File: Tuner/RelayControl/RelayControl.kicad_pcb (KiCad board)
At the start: 2 copper layers, 99.1 x 99.6 mm, 180 parts, among them J1 Conn_01x06, J12 Conn_01x01, J13 Conn_01x01, J14 Conn_01x01, J2 Conn_02x16_Odd_Even, J3 Conn_01x06, J4 Conn_01x01, J5 Conn_01x01, J6 Conn_01x01, J7 Conn_01x01, J8 Conn_02x16_Odd_Even, J9 Conn_01x01, U1 MCP23017, U2 ULN2803A, U3 ULN2803A, U4 MCP23017, U5 ULN2803A, U6 ULN2803A

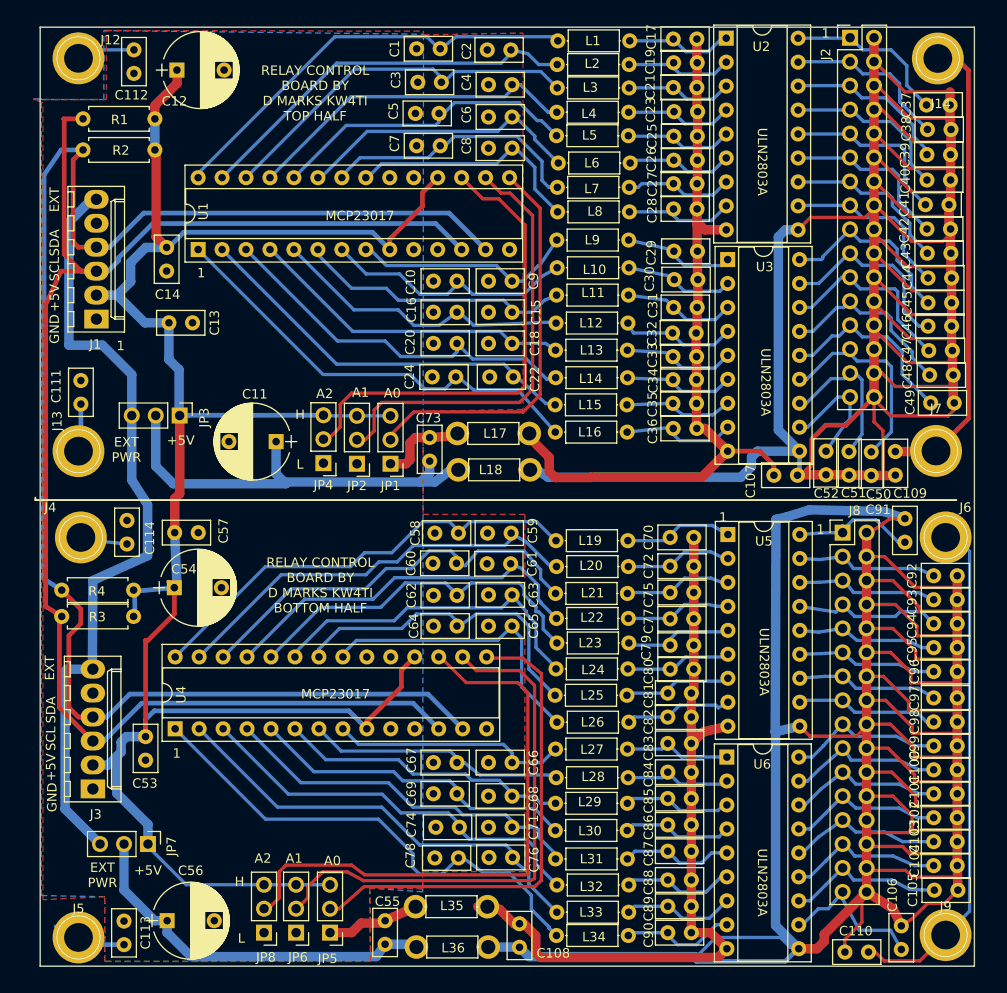
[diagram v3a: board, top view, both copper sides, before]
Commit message: JLCPCB order 09232018 - improved grounding - improved I2C cabling - NEO7M port - support for common mode chokes - relay board now has capacitors on all coils
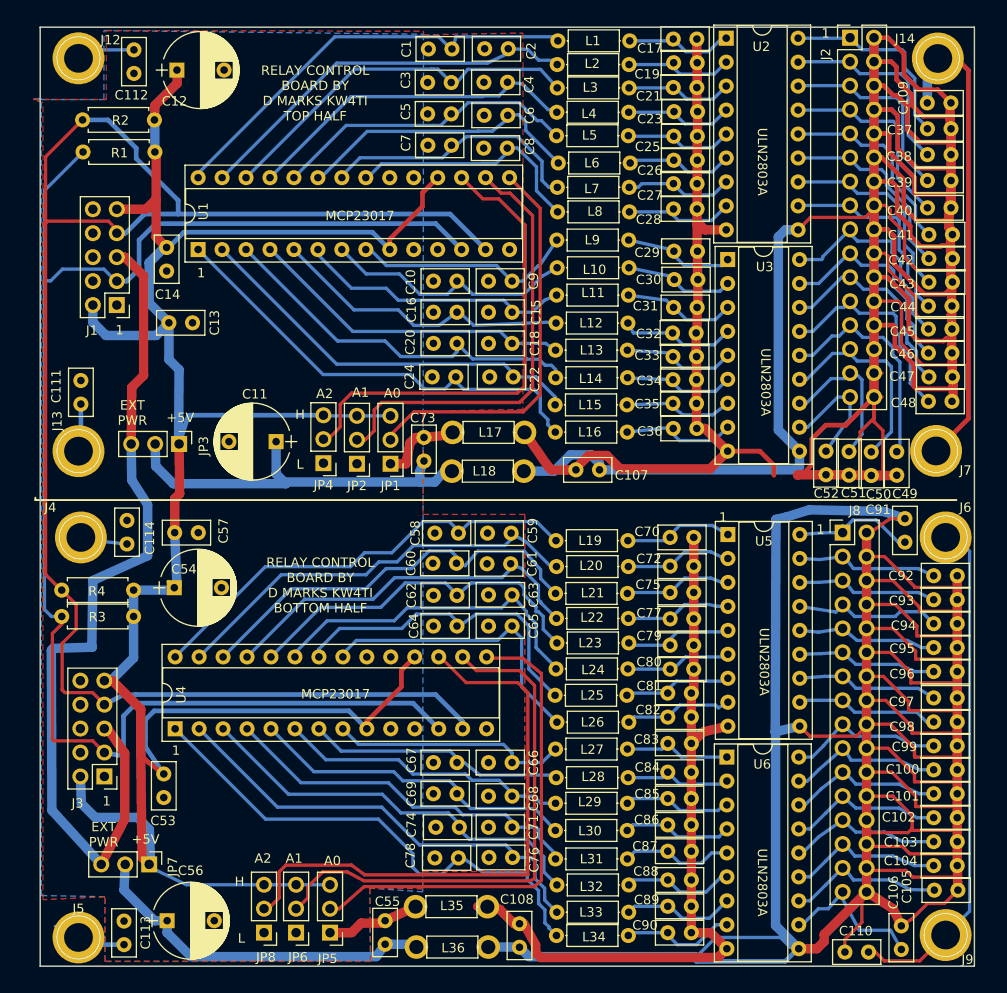
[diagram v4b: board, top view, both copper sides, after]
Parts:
- J1, J3: value Conn_01x06 -> Conn_02x05_Odd_Even; footprint Connectors_Molex:Molex_KK-6410-06_06x2.54mm_Straight -> Pin_Headers:Pin_Header_Straight_2x05_Pitch2.54mm
- moved C109 39.9 mm to (148.4, 57.7), turned to 180 degrees
- moved C107 21.0 mm to (108.6, 96.6)
- moved C49 6.30 mm to (142.6, 94.7), turned to 270 degrees
- moved C53 4.41 mm to (64.9, 131.4)
- moved R1 3.52 mm to (64.0, 62.9)
- moved C41 3.20 mm to (146.1, 71.7)
- moved R2 3.19 mm to (63.9, 59.5)
- moved C42 3.14 mm to (146.1, 74.2)
- moved C43 3.07 mm to (146.1, 76.7)
- moved JP3 3.02 mm to (66.5, 93.9)
- moved C44 2.97 mm to (146.0, 79.2)
- moved C40 2.95 mm to (145.9, 68.8)
- moved C46 2.85 mm to (146.0, 84.2)
- moved C48 2.80 mm to (146.0, 89.4)
- moved C47 2.79 mm to (146.1, 86.8)
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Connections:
- J1 pad 4: SDA -> GND
- J1 pad 5: (no net) -> EXTPWR
- J1 pad 6: EXTPWR -> GND
- J3 pad 4: SDA -> GND
- J3 pad 5: (no net) -> EXTPWR
- J3 pad 6: EXTPWR -> GND
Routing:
- net Net-(C107-Pad2): track 311.8 -> 362.5 mm
- net +5V: track 225.7 -> 252.2 mm
- net EXTPWR: track 83.3 -> 92.9 mm
- net SDA: track 166.7 -> 175.6 mm
- net SCL: track 159.1 -> 165.7 mm
- net RLYPWR: track 46.4 -> 42.5 mm
- net Net-(C49-Pad1): track 20.1 -> 23.7 mm
- net Net-(C39-Pad1): track 17.9 -> 21.5 mm
- net Net-(C38-Pad1): track 17.8 -> 21.4 mm
- net Net-(C43-Pad1): track 18.2 -> 21.6 mm
- net Net-(C48-Pad1): track 19.6 -> 23.0 mm
- net Net-(C40-Pad1): track 18.3 -> 21.6 mm
- net Net-(C37-Pad1): track 17.8 -> 21.1 mm
- net Net-(C45-Pad1): track 19.8 -> 23.1 mm
- net Net-(C44-Pad1): track 18.6 -> 21.8 mm
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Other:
- board text removed: "EXT"
- board text removed: "GND"
- board text removed: "SCL"
- board text removed: "SDA"

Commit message: Relay boards changed to have coil terminals all on same side
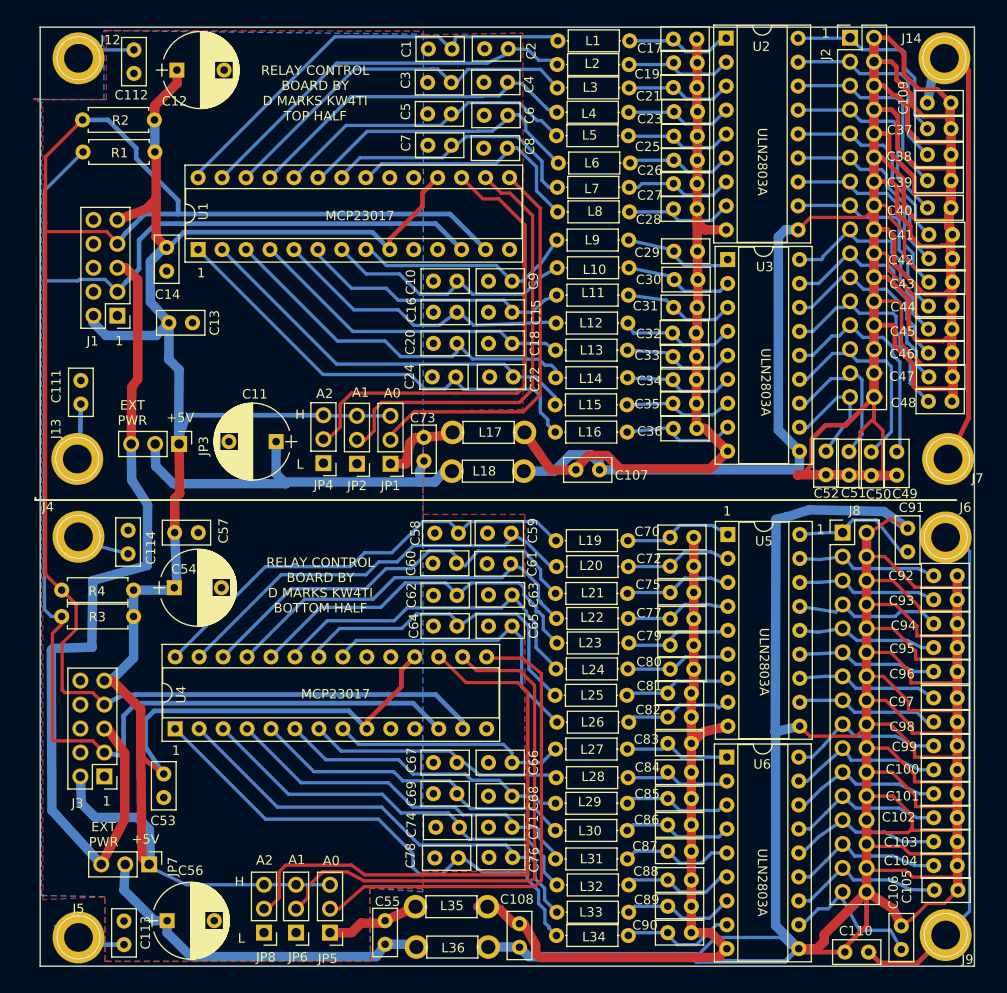
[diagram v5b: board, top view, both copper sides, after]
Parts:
- moved J7 1.53 mm to (148.1, 95.5)
- moved J1 1.13 mm to (60.0, 80.3)
- moved C91 1.06 mm to (143.8, 105.3)
- moved C114 1.05 mm to (61.1, 105.5)
- moved J13 0.84 mm to (55.8, 95.5)
- moved J14 0.70 mm to (147.7, 53.0)
- moved J4 0.26 mm to (55.9, 103.7)
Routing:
- net Net-(C100-Pad2): track 379.7 -> 386.7 mm
- net Net-(C107-Pad1): track 83.0 -> 76.4 mm
- net +5V: track 252.2 -> 251.0 mm
- net EXTPWR: track 92.9 -> 91.8 mm
- net Net-(C91-Pad1): track 13.6 -> 14.5 mm
- net Net-(C110-Pad1): track 54.6 -> 55.5 mm
- net Net-(C111-Pad2): track 5.15 -> 5.98 mm
- net Net-(C114-Pad1): track 6.46 -> 7.03 mm

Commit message: Changed over yet more to BNC
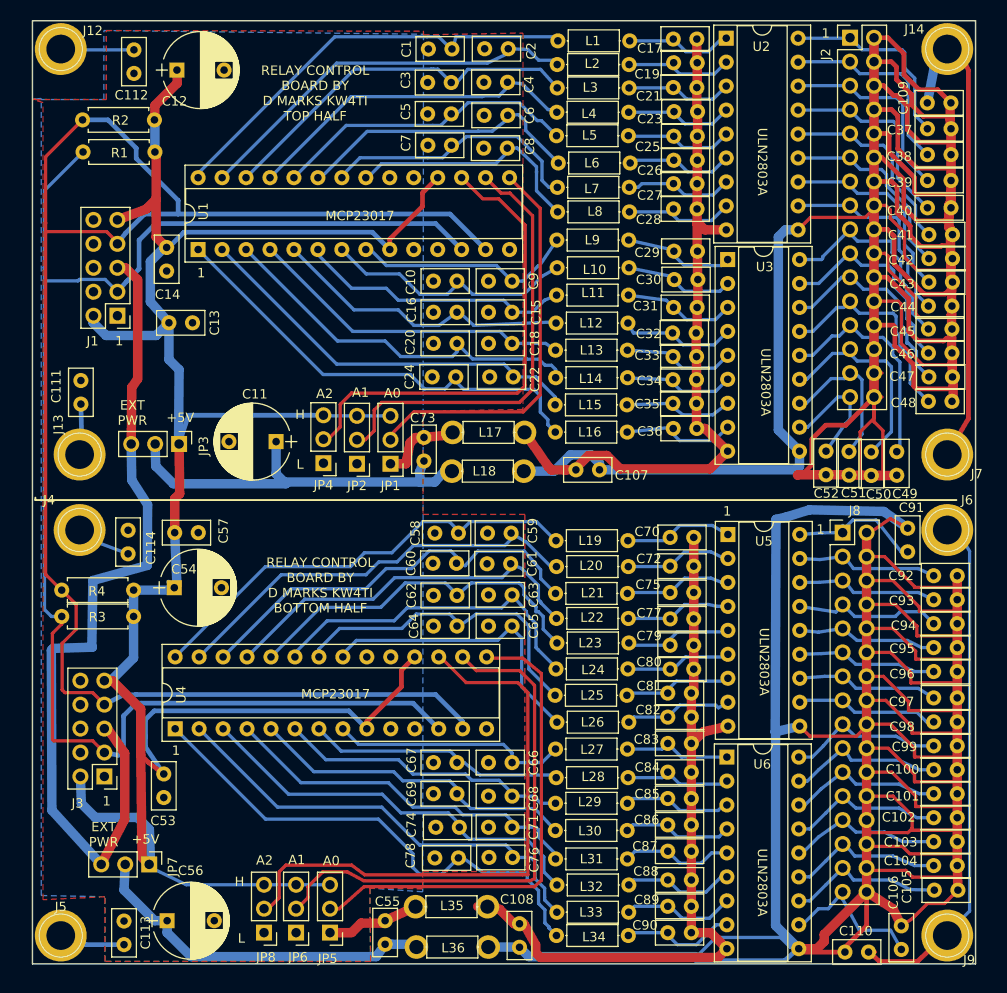
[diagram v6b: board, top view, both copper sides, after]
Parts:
- moved J12 2.12 mm to (54.0, 52.0)
- moved J5 1.89 mm to (54.0, 146.0)
- moved J14 1.03 mm to (148.0, 52.0)
- moved J6 0.80 mm to (148.0, 103.0)
- moved J4 0.73 mm to (56.0, 103.0)
- moved J13 0.53 mm to (56.0, 95.0)
- moved J7 0.47 mm to (148.0, 95.0)
- moved J9 0.18 mm to (148.0, 146.0)
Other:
- board size 99.1 x 99.6 mm -> 100 x 100 mm
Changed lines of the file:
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@@
     (links 425)
     (no_connects 0)
-    (area 48.700818 47.9952 152.57562 150.8094)
+    (area 48.700818 47.9952 152.82962 150.8094)
     (thickness 1.6)
     (drawings 37)
@@
     (pad_to_mask_clearance 0.2)
     (aux_axis_origin 0 0)
-    (grid_origin 103.632 154.0764)
     (visible_elements 7FFFFFFF)
     (pcbplotparams
@@
   )
   (module Connectors:1pin (layer F.Cu)
-    (at 55.88 52.9844)
+    (at 54 52)
     (descr "module 1 pin (ou trou mecanique de percage)")
     (tags DEV)
@@
   )
   (module Connectors:1pin (layer F.Cu)
-    (at 55.753 95.4659)
+    (at 56 95)
     (descr "module 1 pin (ou trou mecanique de percage)")
     (tags DEV)
@@
   )
   (module Connectors:1pin (layer F.Cu)
-    (at 147.701 52.9844)
+    (at 148 52)
     (descr "module 1 pin (ou trou mecanique de percage)")
     (tags DEV)
@@
   )
   (module Connectors:1pin (layer F.Cu)
-    (at 148.082 95.4659)
+    (at 148 95)
     (descr "module 1 pin (ou trou mecanique de percage)")
     (tags DEV)
@@
   )
   (module Connectors:1pin (layer F.Cu)
-    (at 55.88 103.7209)
+    (at 56 103)
     (descr "module 1 pin (ou trou mecanique de percage)")
     (tags DEV)
@@
   )
   (module Connectors:1pin (layer F.Cu)
-    (at 55.88 146.2024)
+    (at 54 146)
     (descr "module 1 pin (ou trou mecanique de percage)")
     (tags DEV)
@@
   )
   (module Connectors:1pin (layer F.Cu)
-    (at 147.828 103.7844)
+    (at 148 103)
     (descr "module 1 pin (ou trou mecanique de percage)")
     (tags DEV)
@@
   )
   (module Connectors:1pin (layer F.Cu)
-    (at 147.828 145.9484)
+    (at 148 146)
     (descr "module 1 pin (ou trou mecanique de percage)")
     (tags DEV)
@@
     )
   )
+  (gr_line (start 51 149) (end 51 49) (angle 90) (layer Edge.Cuts) (width 0.15))
+  (gr_line (start 151 149) (end 51 149) (angle 90) (layer Edge.Cuts) (width 0.15))
+  (gr_line (start 151 49) (end 151 149) (angle 90) (layer Edge.Cuts) (width 0.15))
+  (gr_line (start 51 49) (end 151 49) (angle 90) (layer Edge.Cuts) (width 0.15))
   (gr_text 1 (at 58.8645 131.7498) (layer F.SilkS)
     (effects (font (size 1 1) (thickness 0.15)))
   )
-  (gr_line (start 51.816 149.2504) (end 51.816 49.6824) (angle 90) (layer Edge.Cuts) (width 0.15))
-  (gr_line (start 150.876 149.2504) (end 51.816 149.2504) (angle 90) (layer Edge.Cuts) (width 0.15))
-  (gr_line (start 150.876 49.6824) (end 150.876 149.2504) (angle 90) (layer Edge.Cuts) (width 0.15))
-  (gr_line (start 51.816 49.6824) (end 150.876 49.6824) (angle 90) (layer Edge.Cuts) (width 0.15))
   (gr_text 1 (at 68.8848 75.7428) (layer F.SilkS)
     (effects (font (size 1 1) (thickness 0.15)))
@@
   (segment (start 120.904 148.2344) (end 121.35104 148.2344) (width 0.35) (layer B.Cu) (net 95))
   (segment (start 121.35104 148.2344) (end 121.412 148.2344) (width 0.35) (layer B.Cu) (net 95))
-  (segment (start 130.81 148.7424) (end 121.412 148.7424) (width 0.5) (layer B.Cu) (net 95))
-  (segment (start 121.412 148.7424) (end 120.904 148.2344) (width 0.5) (layer B.Cu) (net 95))
-  (segment (start 132.156 147.3964) (end 130.81 148.7424) (width 0.5) (layer B.Cu) (net 95) (status 10))
+  (segment (start 130.7592 148.6662) (end 121.3612 148.6662) (width 0.5) (layer B.Cu) (net 95))
+  (segment (start 121.3612 148.6662) (end 120.904 148.2344) (width 0.5) (layer B.Cu) (net 95))
+  (segment (start 132.156 147.3964) (end 130.7592 148.6662) (width 0.5) (layer B.Cu) (net 95) (status 10))
   (segment (start 121.412 148.2344) (end 123.444 146.2024) (width 0.35) (layer B.Cu) (net 95))
   (segment (start 131.318 147.2184) (end 132.074 147.2184) (width 0.35) (layer B.Cu) (net 95) (status 20))
@@
   (segment (start 147.701 52.9844) (end 149.6876 52.9844) (width 0.5) (layer F.Cu) (net 114) (status 30))
   (segment (start 149.6876 52.9844) (end 150.241 54.2544) (width 0.5) (layer F.Cu) (net 114) (status 10))
-  (segment (start 150.241 91.186) (end 148.082 95.4659) (width 0.5) (layer F.Cu) (net 114) (status 20))
+  (segment (start 150.241 91.186) (end 148 95) (width 0.5) (layer F.Cu) (net 114) (status 20))
   (segment (start 150.241 54.2544) (end 150.241 91.186) (width 0.5) (layer F.Cu) (net 114))
-  (segment (start 148.0166 95.5313) (end 148.082 95.4659) (width 1) (layer F.Cu) (net 114) (status 30))
+  (segment (start 147.9346 95.0654) (end 148 95) (width 1) (layer F.Cu) (net 114) (status 30))
   (segment (start 147.513 53.1724) (end 147.701 52.9844) (width 1) (layer B.Cu) (net 114) (status 30))
   (segment (start 139.6492 147.7518) (end 139.7254 147.7518) (width 0.5) (layer F.Cu) (net 115))
-  (segment (start 139.7254 147.7518) (end 140.8811 148.9075) (width 0.5) (layer F.Cu) (net 115))
-  (segment (start 144.8689 148.9075) (end 147.828 145.9484) (width 0.5) (layer F.Cu) (net 115))
-  (segment (start 140.8811 148.9075) (end 144.8689 148.9075) (width 0.5) (layer F.Cu) (net 115))
+  (segment (start 139.7254 147.7518) (end 140.8303 148.7551) (width 0.5) (layer F.Cu) (net 115))
+  (segment (start 144.8181 148.7551) (end 147.828 145.9484) (width 0.5) (layer F.Cu) (net 115))
+  (segment (start 140.8303 148.7551) (end 144.8181 148.7551) (width 0.5) (layer F.Cu) (net 115))
   (segment (start 139.6492 147.7518) (end 140.3858 147.7518) (width 0.35) (layer F.Cu) (net 115))
-  (segment (start 147.828 103.7844) (end 148.8948 103.7844) (width 0.35) (layer B.Cu) (net 115))
-  (segment (start 148.8948 103.7844) (end 150.368 105.2576) (width 0.35) (layer B.Cu) (net 115))
+  (segment (start 148 103) (end 149.0668 103) (width 0.35) (layer B.Cu) (net 115) (status 30))
+  (segment (start 149.0668 103) (end 150.368 105.2576) (width 0.35) (layer B.Cu) (net 115) (status 10))
   (segment (start 150.368 105.2576) (end 150.368 143.4084) (width 0.35) (layer B.Cu) (net 115))
   (segment (start 150.368 143.4084) (end 147.828 145.9484) (width 0.35) (layer B.Cu) (net 115))
-  (segment (start 56.134 89.6474) (end 56.007 95.2119) (width 0.5) (layer B.Cu) (net 116) (status 20))
-  (segment (start 56.007 95.2119) (end 55.753 95.4659) (width 0.5) (layer B.Cu) (net 116) (status 30))
+  (segment (start 56.134 89.6474) (end 56.254 94.746) (width 0.5) (layer B.Cu) (net 116) (status 20))
+  (segment (start 56.254 94.746) (end 56 95) (width 0.5) (layer B.Cu) (net 116) (status 30))
   (segment (start 56.134 89.6474) (end 56.134 89.7001) (width 0.35) (layer B.Cu) (net 116) (status 30))
   (segment (start 61.7601 52.0846) (end 55.6238 52.0846) (width 0.35) (layer B.Cu) (net 117) (status 20))
@@
   (segment (start 56.642 146.9644) (end 55.88 146.2024) (width 0.5) (layer B.Cu) (net 118))
   (segment (start 53.4289 145.0213) (end 54.356 145.9484) (width 0.35) (layer B.Cu) (net 118))
-  (segment (start 61.1378 105.5243) (end 54.39664 103.76154) (width 0.35) (layer B.Cu) (net 119) (status 20))
-  (segment (start 54.39664 103.76154) (end 54.356 103.7209) (width 0.35) (layer B.Cu) (net 119) (status 30))
+  (segment (start 61.1378 105.5243) (end 54.51664 103.04064) (width 0.35) (layer B.Cu) (net 119) (status 20))
+  (segment (start 54.51664 103.04064) (end 54.476 103) (width 0.35) (layer B.Cu) (net 119) (status 30))
   (zone (net 1) (net_name GND) (layer F.Cu) (hatch edge 0.508)
     (connect_pads (clearance 0.5))

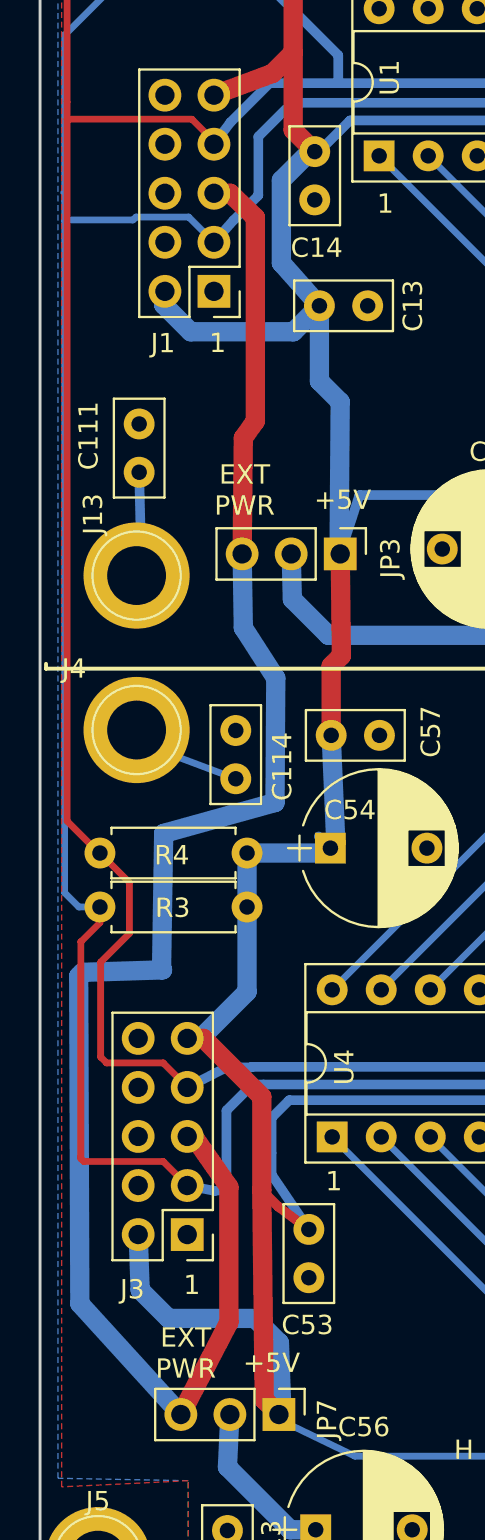
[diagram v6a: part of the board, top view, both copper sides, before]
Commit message: Changed I2C cable pinoutgit add Tunergit add Tuner Also added ICOM rig support
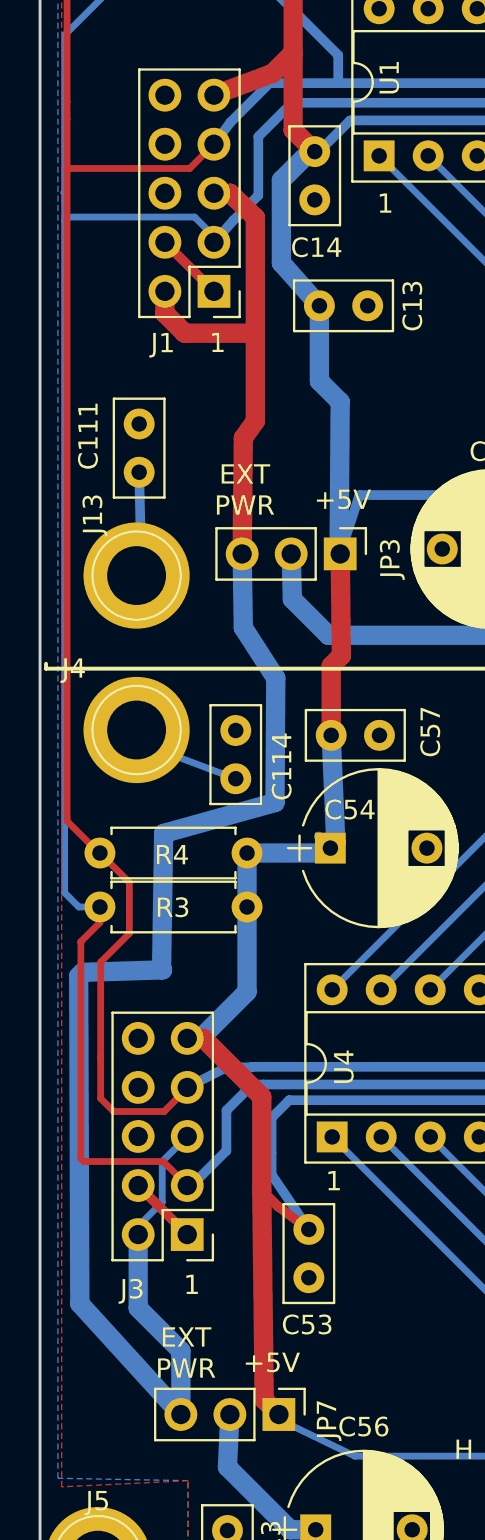
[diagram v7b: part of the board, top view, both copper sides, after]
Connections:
- J1 pad 2: +5V -> EXTPWR
- J3 pad 2: +5V -> EXTPWR
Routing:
- net +5V: track 251.0 -> 226.4 mm
- net GND: track 19.6 -> 26.8 mm
- net EXTPWR: track 91.8 -> 98.8 mm
- net SDA: track 176.0 -> 178.4 mm
- net SCL: track 165.9 -> 164.8 mm
